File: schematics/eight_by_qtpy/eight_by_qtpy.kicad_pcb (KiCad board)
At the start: 2 copper layers, 174 x 44.4 mm, 44 parts, among them J1 Conn_01x08, SW1 SW_Push_45deg, SW2 SW_Push_45deg, SW3 SW_Push_45deg, SW4 SW_Push_45deg, SW5 SW_Push_45deg, SW6 SW_Push_45deg, SW7 SW_Push_45deg, SW8 SW_Push_45deg, U1 74HC4051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

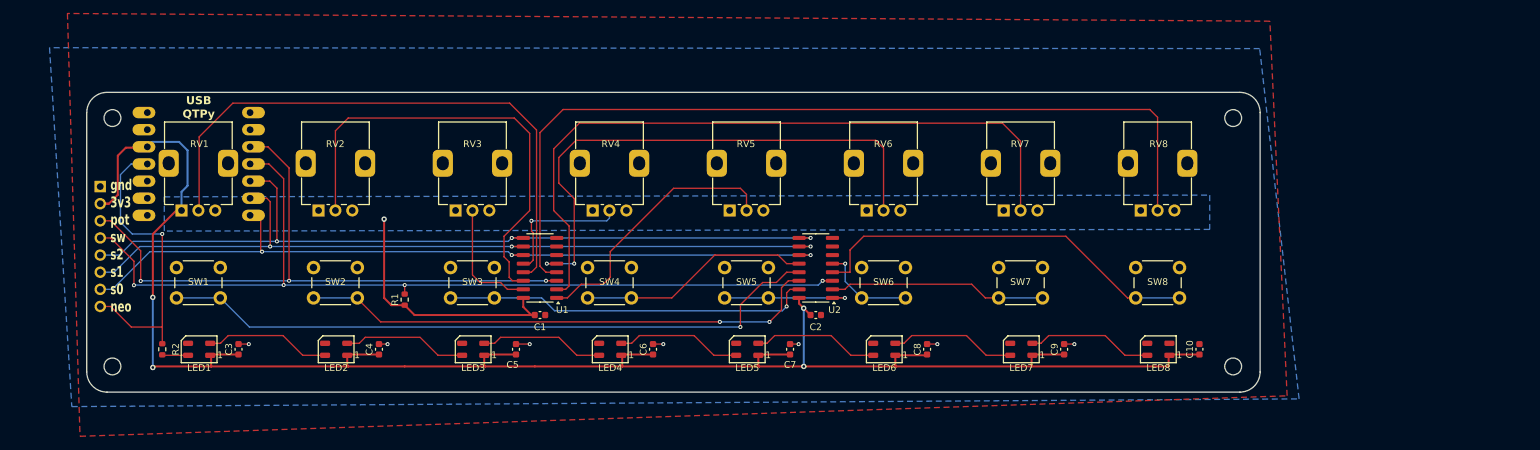
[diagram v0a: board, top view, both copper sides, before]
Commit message: add two extra buttons & LEDs if using a QTpy
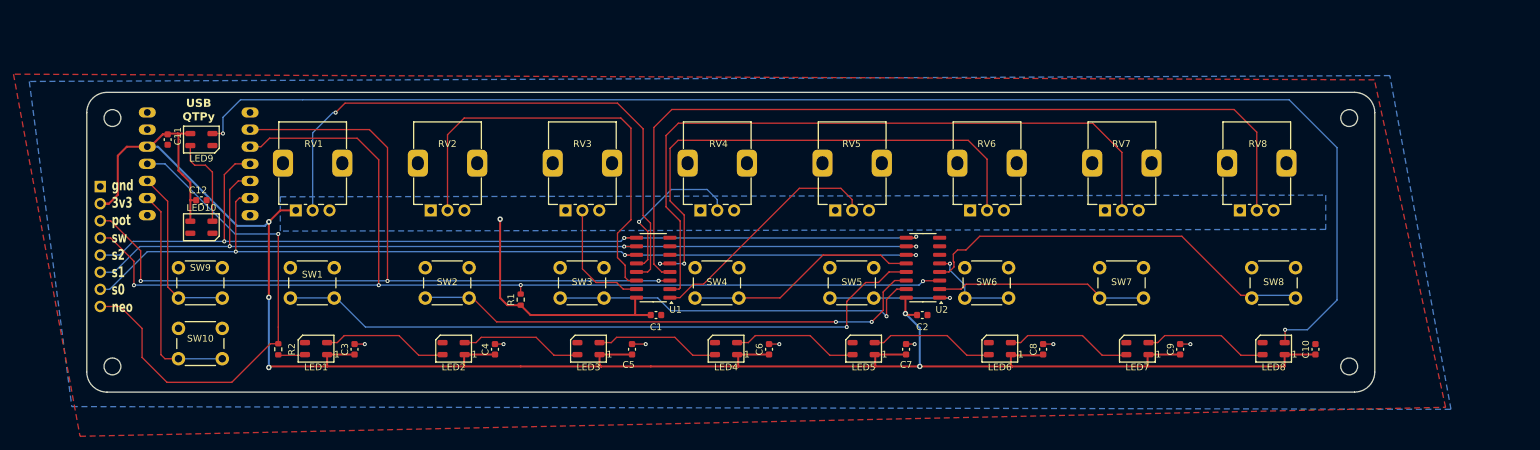
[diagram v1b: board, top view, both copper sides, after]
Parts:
- added C11: 100n, Capacitor_SMD:C_0603_1608Metric, F.Cu at (37.4, 32.4)
- added C12: 100n, Capacitor_SMD:C_0603_1608Metric, F.Cu at (42.4, 41.4)
- added LED10: WS2812B, LED_SMD:LED_WS2812B-Mini_PLCC4_3.5x3.5mm, F.Cu at (42.4, 45.4)
- added LED9: WS2812B, LED_SMD:LED_WS2812B-Mini_PLCC4_3.5x3.5mm, F.Cu at (42.4, 32.4)
- added SW10: SW_Push_45deg, Button_Switch_THT:SW_PUSH_6mm_H7.3mm, F.Cu at (39.0, 60.4)
- added SW9: SW_Push_45deg, Button_Switch_THT:SW_PUSH_6mm_H7.3mm, F.Cu at (39.0, 51.4)
- U3: footprint todbot_eagle2023:QTPY_TH -> todbot_eagle2023:QTPY_TH_HEADERSOCKET
- moved LED2 17.4 mm to (79.8, 63.4)
- moved LED1 17.3 mm to (59.4, 63.4)
- moved LED5 17.3 mm to (140.6, 63.4)
- moved LED7 17.2 mm to (181.2, 63.4)
- moved SW8 17.2 mm to (198.2, 51.4)
- moved C7 17.2 mm to (146.9, 63.5)
- moved C1 17.2 mm to (109.8, 58.4)
- moved C4 17.2 mm to (85.9, 63.5)
- moved C6 17.2 mm to (126.6, 63.5)
- moved R1 17.2 mm to (89.7, 56.1)
- moved C3 17.2 mm to (65.1, 63.5)
- moved R2 17.2 mm to (53.8, 63.5)
- moved C10 17.2 mm to (207.6, 63.5)
- moved C5 17.2 mm to (106.3, 63.5)
- moved C8 17.2 mm to (167.2, 63.5)
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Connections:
- LED8 pad 2: unconnected-(LED8-DOUT-Pad2) -> Net-(LED8-DOUT)
- U3 pad A1: unconnected-(U3-9-PadA1) -> /POT
- U3 pad A2: /POT -> /SW
- U3 pad A3: /SW -> /S2
- U3 pad MI: unconnected-(U3-PadMI) -> /SW9
- U3 pad SCK: unconnected-(U3-PadSCK) -> /SW10
- U3 pad SCL: /S1 -> /S0
- U3 pad SDA: /S2 -> /S1
- U3 pad TX: /S0 -> /MIDI_TX
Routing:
- net Net-(LED8-DOUT): track 0.00 -> 207.2 mm, vias 0 -> 2
- net /POT: track 97.6 -> 131.7 mm
- net /SW: track 136.6 -> 170.3 mm
- net /SW10: track 0.00 -> 33.4 mm
- net +3V3: track 308.5 -> 341.1 mm, vias 5 -> 6
- net /NEOPIXEL: track 45.7 -> 76.3 mm
- net /SW9: track 0.00 -> 25.7 mm
- net /S0: track 117.9 -> 136.1 mm
- net /S2: track 121.9 -> 139.8 mm
- net /S1: track 120.0 -> 137.8 mm
- net Net-(LED10-DIN): track 0.00 -> 13.4 mm
- net /POT5: track 39.9 -> 36.2 mm
- net /POT8: track 130.0 -> 126.4 mm
- net /POT4: track 20.7 -> 24.1 mm
- net /POT2: track 67.9 -> 65.2 mm
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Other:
- board size 174 x 44.4 mm -> 191 x 44.4 mm
- board text added: "5v gnd 3v neo sw9 sw10 rx"
- board text added: "a0 pot sw s2 s1 s0 tx"

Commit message: clean up
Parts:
- moved C9 3.74 mm to (183.8, 63.4)
- moved C8 3.42 mm to (163.8, 63.4)
- moved C10 3.40 mm to (204.2, 63.4)
- moved C7 3.10 mm to (143.8, 63.4)
- moved C6 2.78 mm to (123.8, 63.4)
- moved LED8 2.60 mm to (198.8, 63.4)
- moved SW8 2.55 mm to (195.6, 51.4)
- moved C5 2.46 mm to (103.8, 63.4)
- moved LED7 2.40 mm to (178.8, 63.4)
- moved C4 2.14 mm to (83.8, 63.4)
- moved LED6 2.00 mm to (158.8, 63.4)
- moved LED5 1.80 mm to (138.8, 63.4)
- moved LED4 1.40 mm to (118.8, 63.4)
- moved C3 1.31 mm to (63.8, 63.4)
- moved LED2 1.00 mm to (78.8, 63.4)
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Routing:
- net +3V3: track 341.1 -> 336.6 mm
- net /SW8: track 60.0 -> 58.0 mm
- net Net-(LED8-DOUT): track 207.2 -> 209.2 mm
- net GND: track 10.7 -> 9.08 mm
- net /POT: track 131.7 -> 131.1 mm

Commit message: clean up
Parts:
- added J2: AudioJack4, todbot_stuff:Jack_3.5mm_PJ320D_Horizontal, B.Cu at (188.8, 27.8)
- added R3: 10, Resistor_SMD:R_0603_1608Metric, F.Cu at (172.4, 24.8)
- added R4: 33, Resistor_SMD:R_0603_1608Metric, F.Cu at (178.4, 24.8)
- moved C11 6.28 mm to (42.4, 28.6), turned to 0 degrees
- moved U3 3.98 mm to (42.0, 32.0)
- moved H1 3.81 mm to (29.2, 25.4)
- moved H3 3.81 mm to (212.6, 25.4)
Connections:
- U3 pad TX: /MIDI_TX -> /MIDI_OUT
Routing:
- net /MIDI_OUT: track 0.00 -> 137.6 mm, vias 0 -> 1
- net +3V3: track 336.6 -> 369.0 mm, vias 6 -> 7
- net Net-(J2-PadT): track 0.00 -> 15.2 mm, vias 0 -> 1
- net Net-(LED8-DOUT): track 209.2 -> 198.7 mm, vias 2 -> 4
- net Net-(J2-PadR1): track 0.00 -> 7.50 mm, vias 0 -> 1
- net /SW9: track 25.7 -> 30.6 mm
- net /SW10: track 33.4 -> 38.3 mm
- net /S0: track 136.1 -> 140.0 mm
- net /S2: track 139.8 -> 143.7 mm
- net /S1: track 137.8 -> 141.4 mm
- net /POT1: track 87.6 -> 90.5 mm
- net /NEOPIXEL: track 76.3 -> 78.4 mm
- net /POT: track 131.1 -> 132.8 mm
- net Net-(LED1-DOUT): track 18.8 -> 17.7 mm
- net Net-(LED10-DIN): track 13.4 -> 14.4 mm
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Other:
- board size 191 x 44.4 mm -> 191 x 48.4 mm

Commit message: rethinking eight_by_qtpy
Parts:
- moved C12 2.00 mm to (42.4, 39.4)
- moved LED10 2.00 mm to (42.4, 43.4)
- moved C1 1.01 mm to (108.8, 58.4)
- moved U1 0.60 mm to (108.8, 51.4)
- moved U2 0.60 mm to (148.8, 51.4)
- moved C2 0.50 mm to (148.8, 58.4)
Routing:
- net /POT6: track 79.1 -> 71.7 mm
- net /S0: track 140.0 -> 137.5 mm
- net /POT8: track 126.4 -> 128.6 mm
- net Net-(LED10-DIN): track 14.4 -> 12.4 mm
- net +3V3: track 369.0 -> 367.6 mm
- net /S2: track 143.7 -> 142.4 mm
- net /SW4: track 34.4 -> 35.6 mm
- net /S1: track 141.4 -> 140.3 mm
- net /POT5: track 36.2 -> 35.3 mm
- net /POT7: track 104.0 -> 104.9 mm
- net /POT4: track 24.1 -> 23.2 mm
- net /SW5: track 19.7 -> 18.9 mm
- net /NEOPIXEL: track 78.4 -> 77.7 mm
- net /SW8: track 58.0 -> 58.6 mm
- net /POT2: track 65.2 -> 65.8 mm
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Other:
- board text added: "1"
- board text added: "2"
- board text added: "3"
- board text added: "4"
- board text added: "5"
- board text added: "6"
- board text added: "7"
- board text added: "8"
- board text added: "A"
- board text added: "B"
- board text added: "MIDI OUT"
- board text added: "MIDI OUT TRS-A"
- board text added: "[>]"
- board text added: "a0 pot sw s2 s1 s0 tx midi"
- board text added: "edit"
- board text added: "eight_by_qtpy 25 Oct 2024 - @todbot github.com/todbot/eight_by"
- board text added: "midi tx"
- board text removed: "a0 pot sw s2 s1 s0 tx"

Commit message: rethinking eight_by_qtpy
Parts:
- moved J1 44.6 mm to (69.4, 24.4), turned to -90 degrees
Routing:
- net /POT: track 132.8 -> 95.7 mm, vias 3 -> 2
- net /NEOPIXEL: track 77.7 -> 104.3 mm, vias 1 -> 2
- net +3V3: track 367.6 -> 389.6 mm
- net /SW: track 170.9 -> 159.6 mm, vias 4 -> 3
- net /S2: track 142.4 -> 151.6 mm, vias 3 -> 4
- net /S1: track 140.3 -> 147.1 mm, vias 3 -> 4
- net /POT1: track 90.4 -> 84.3 mm
- net /MIDI_OUT: track 137.6 -> 132.2 mm
- net /S0: track 137.5 -> 141.6 mm, vias 3 -> 4
- net /POT2: track 65.8 -> 65.0 mm, vias 0 -> 2
- net /SW9: track 30.6 -> 31.3 mm
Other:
- board text added: "play"
- board text removed: "[>]"

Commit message: new silkscreen
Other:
- board text added: "@todbot"
- board text added: "eight_by"

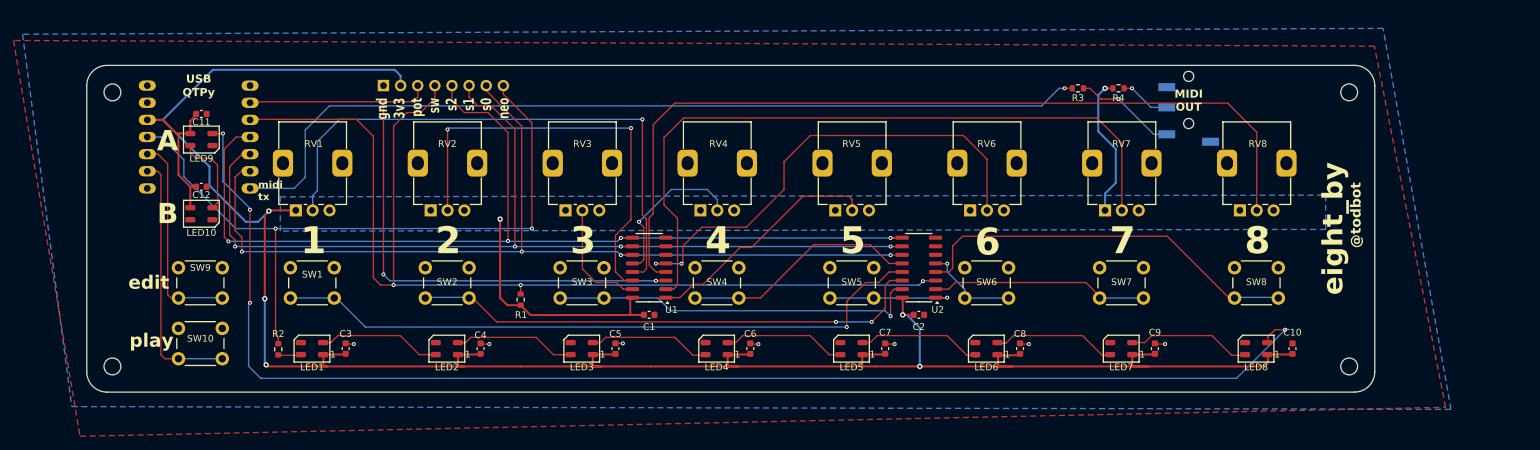
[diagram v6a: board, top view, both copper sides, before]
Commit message: refactor eight_by_qtpy to use 12mm switches instead of std 6mm tact
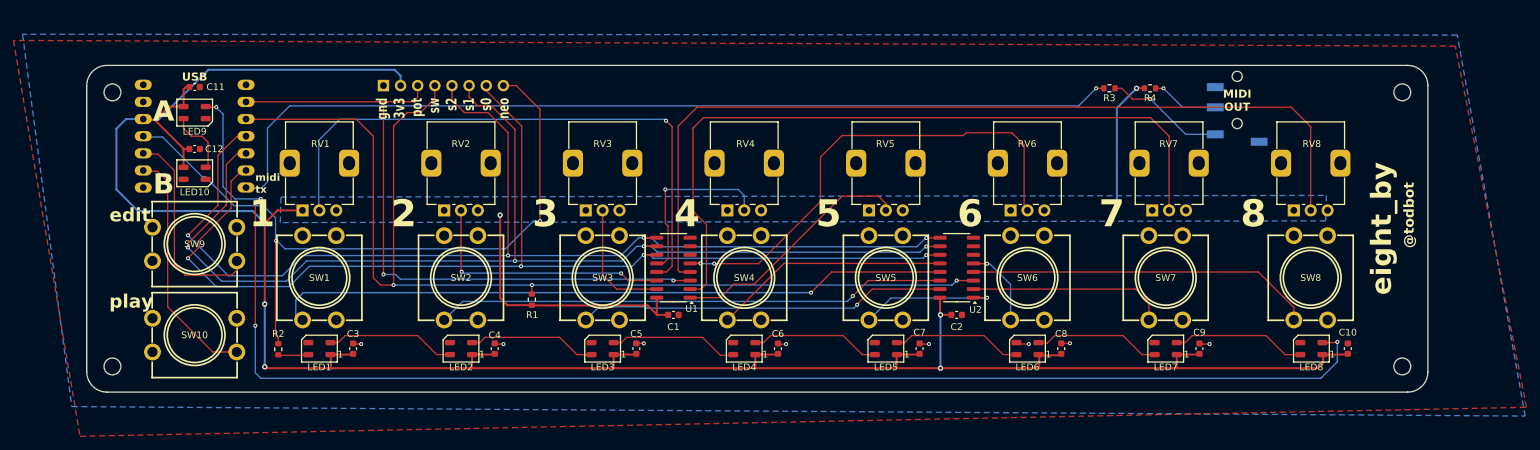
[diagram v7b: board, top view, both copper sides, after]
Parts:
- SW1, SW10, SW2, SW3, SW4, SW5, SW6, SW7, SW8, SW9: value SW_Push_45deg -> TC-1103-C-D; footprint Button_Switch_THT:SW_PUSH_6mm_H7.3mm -> easyeda2kicad:SW-TH_4P-L12.0-W12.0-P5.00-LS12.5
- moved SW8 11.4 mm to (206.9, 52.9), turned to -90 degrees
- moved SW7 9.91 mm to (185.4, 52.9), turned to -90 degrees
- moved SW6 9.42 mm to (164.9, 52.9), turned to -90 degrees
- moved SW5 8.43 mm to (143.9, 52.9), turned to -90 degrees
- moved C10 8.20 mm to (212.4, 63.4)
- moved LED8 8.20 mm to (207.0, 63.4)
- moved RV8 8.00 mm to (204.4, 42.9)
- moved H3 7.88 mm to (220.5, 25.4)
- moved H4 7.88 mm to (220.5, 66.0)
- moved SW4 7.45 mm to (122.9, 52.9), turned to -90 degrees
- moved J2 7.20 mm to (196.0, 27.8)
- moved RV7 7.00 mm to (183.4, 42.9)
- moved C9 6.60 mm to (190.4, 63.4)
- moved LED7 6.60 mm to (185.4, 63.4)
- moved SW3 6.48 mm to (101.9, 52.9), turned to -90 degrees
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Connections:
- SW1 pad 2: /SW1 -> unconnected-(SW1-Pad2)
- SW10 pad 2: /SW10 -> unconnected-(SW10-Pad2)
- SW2 pad 2: /SW2 -> unconnected-(SW2-Pad2)
- SW3 pad 2: /SW3 -> unconnected-(SW3-Pad2)
- SW4 pad 2: /SW4 -> unconnected-(SW4-Pad2)
- SW5 pad 2: /SW5 -> unconnected-(SW5-Pad2)
- SW6 pad 2: /SW6 -> unconnected-(SW6-Pad2)
- SW7 pad 2: /SW7 -> unconnected-(SW7-Pad2)
- SW8 pad 2: /SW8 -> unconnected-(SW8-Pad2)
- SW9 pad 2: /SW9 -> unconnected-(SW9-Pad2)
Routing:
- net /POT2: track 65.0 -> 38.6 mm
- net /S0: track 141.6 -> 164.1 mm
- net /S1: track 147.1 -> 167.3 mm
- net /S2: track 151.6 -> 171.6 mm
- net Net-(LED8-DOUT): track 199.1 -> 213.2 mm
- net +3V3: track 389.6 -> 398.9 mm
- net /SW8: track 58.6 -> 51.6 mm
- net /MIDI_OUT: track 132.2 -> 137.4 mm
- net /POT7: track 104.9 -> 110.0 mm
- net /SW: track 159.6 -> 164.7 mm
- net /POT1: track 84.3 -> 87.9 mm
- net /POT4: track 23.2 -> 26.7 mm
- net /NEOPIXEL: track 104.3 -> 107.7 mm
- net /POT8: track 128.6 -> 131.9 mm
- net /POT: track 95.7 -> 98.9 mm
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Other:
- board size 191 x 48.4 mm -> 198.9 x 48.4 mm

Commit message: clea up eight_by_qtpy refactor layout
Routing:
- net GND: track 11.1 -> 1.98 mm, vias 8 -> 0
- net /POT1: track 87.9 -> 82.1 mm
- net /POT4: track 26.7 -> 21.5 mm
- net /SW10: track 35.3 -> 38.2 mm
- net /SW3: track 54.6 -> 56.4 mm
- net /SW1: track 100.2 -> 98.8 mm
- net /S0: track 164.1 -> 164.7 mm
- net +3V3: track 398.9 -> 399.5 mm
- net /S1: track 167.3 -> 167.9 mm
